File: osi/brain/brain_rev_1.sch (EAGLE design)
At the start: 10 parts, among them IC1 TINY24/44/84-PU

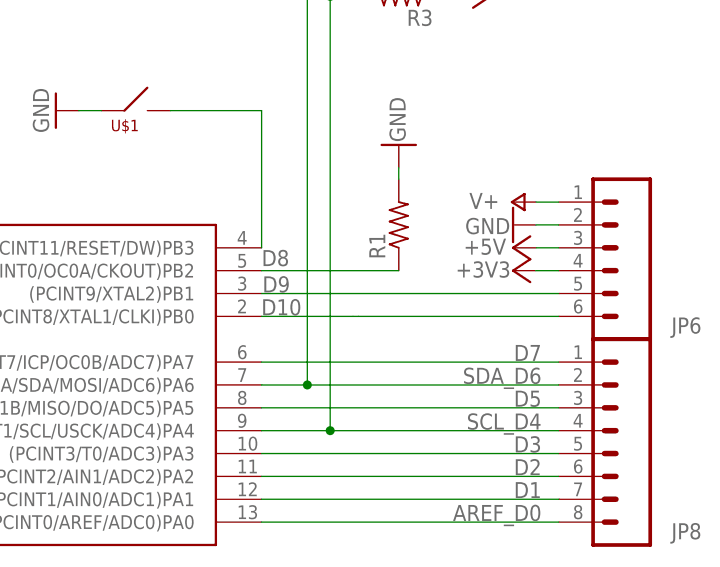
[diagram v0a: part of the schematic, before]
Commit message: D9 -> D8 for INT0
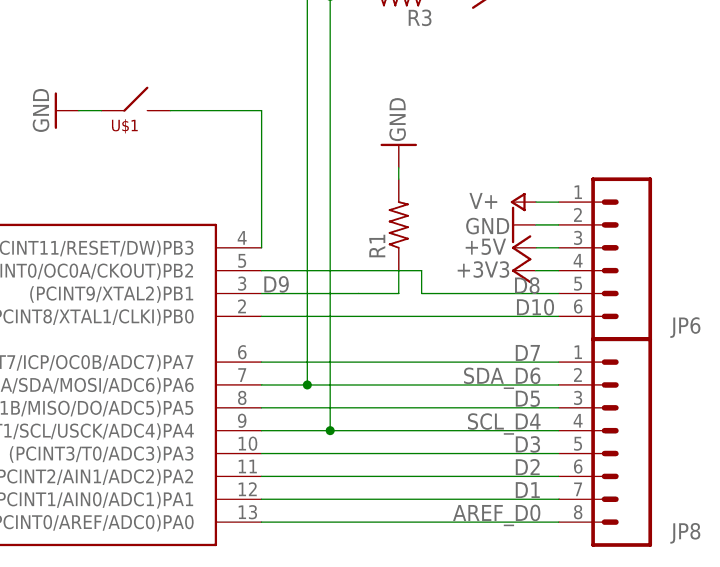
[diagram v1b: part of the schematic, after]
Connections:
- net D8: now also JP6.5; no longer R1.1
- net D9: now also R1.1; no longer JP6.5
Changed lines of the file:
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@@
 <wire x1="88.9" y1="58.42" x2="99.06" y2="58.42" width="0.1524" layer="91"/>
 <label x="92.075" y="60.325" size="1.778" layer="95" rot="R180"/>
-<pinref part="JP6" gate="G$1" pin="5"/>
+<pinref part="R1" gate="G$1" pin="1"/>
 <wire x1="99.06" y1="58.42" x2="99.695" y2="58.42" width="0.1524" layer="91"/>
-<wire x1="99.695" y1="58.42" x2="121.92" y2="58.42" width="0.1524" layer="91"/>
+<wire x1="99.695" y1="58.42" x2="104.14" y2="58.42" width="0.1524" layer="91"/>
+<wire x1="104.14" y1="58.42" x2="104.14" y2="60.96" width="0.1524" layer="91"/>
 </segment>
 </net>
@@
 <segment>
 <pinref part="IC1" gate="1" pin="(PCINT8/XTAL1/CLKI)PB0"/>
-<wire x1="88.9" y1="55.88" x2="99.06" y2="55.88" width="0.1524" layer="91"/>
-<label x="93.345" y="57.785" size="1.778" layer="95" rot="R180"/>
+<label x="121.539" y="57.785" size="1.778" layer="95" rot="R180"/>
 <pinref part="JP6" gate="G$1" pin="6"/>
-<wire x1="99.06" y1="55.88" x2="99.695" y2="55.88" width="0.1524" layer="91"/>
-<wire x1="99.695" y1="55.88" x2="121.92" y2="55.88" width="0.1524" layer="91"/>
+<wire x1="88.9" y1="55.88" x2="121.92" y2="55.88" width="0.1524" layer="91"/>
 </segment>
 </net>
@@
 <segment>
 <pinref part="IC1" gate="1" pin="(PCINT10/INT0/OC0A/CKOUT)PB2"/>
-<wire x1="88.9" y1="60.96" x2="104.14" y2="60.96" width="0.1524" layer="91"/>
-<pinref part="R1" gate="G$1" pin="1"/>
-<label x="88.9" y="61.468" size="1.778" layer="95"/>
+<wire x1="88.9" y1="60.96" x2="106.68" y2="60.96" width="0.1524" layer="91"/>
+<wire x1="106.68" y1="60.96" x2="106.68" y2="58.42" width="0.1524" layer="91"/>
+<pinref part="JP6" gate="G$1" pin="5"/>
+<wire x1="106.68" y1="58.42" x2="121.92" y2="58.42" width="0.1524" layer="91"/>
+<label x="116.84" y="58.42" size="1.778" layer="95"/>
 </segment>
 </net>

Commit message: FURBY
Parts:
- added U$2: 2.1MMJACKTHM, adafruit:2.1MMJACKTHM
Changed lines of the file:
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@@
 <part name="+3V5" library="supply1" deviceset="+3V3" device=""/>
 <part name="+3V6" library="supply1" deviceset="+3V3" device=""/>
+<part name="U$2" library="adafruit" deviceset="2.1MMJACK" device="THM"/>
 </parts>
 <sheets>
@@
 <attribute name="VALUE" x="116.84" y="96.52" size="1.778" layer="96"/>
 </instance>
+<instance part="U$2" gate="G$1" x="27.94" y="96.52"/>
 </instances>
 <busses>
